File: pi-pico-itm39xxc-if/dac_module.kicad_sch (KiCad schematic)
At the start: 52 parts

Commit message: Working on pico itm interface
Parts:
- removed C? (x2): 1uF, Capacitor_SMD:C_0805_2012Metric, symbol Device:C_Small
- removed C?: 100nF, Capacitor_SMD:C_0805_2012Metric, symbol Device:C_Small
- removed U?: MAX6035xxUR25, Package_TO_SOT_SMD:SOT-23_Handsoldering, symbol Reference_Voltage:MAX6035xxUR25
- added C?: 100nF, Capacitor_SMD:C_0805_2012Metric, symbol Device:C_Small
- added R?: 2k, Resistor_SMD:R_0805_2012Metric, symbol Device:R_Small
- added U?: LM4040DBZ-3, Package_TO_SOT_SMD:SOT-23, symbol Reference_Voltage:LM4040DBZ-3
- C?: value 150nF -> 1uF
- R? (x4): value 30k -> 56k
- R?: value 47k -> 10k
- R? (x4): value 10k -> 24k
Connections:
- net GND: now also C?.2, U?.2 (A)
- net Vdd: now also R?.1
- net at U?.3 (+): now also C?.1, R?.2, U?.1 (K)
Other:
- note added: "Supply info - Vdd: 3.3 V - Vcc: 12 V Analog outputs: - DAC_A1, A2 and A3: 0 V - 10 V - DAC_REF: 3 V [1] Although MCP4922's does not seem to specify some minimum output load, we place a resistor here. This is also done in mikroe's MCP4921 board: https://download.mikroe.com/documents/add-on-boards/click/dac/dac-click-schematic-v100.pdf [2] LM4040's datasheet recommends a 100nF bypass cap at the cat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"
- note removed: "Supply info - Vdd: 3.3 V - Vcc: 12 V Analog outputs: - 0 V - 10 V [1] Although MCP4922's does not seem to specify some minimum output load, we place a resistor here. This is also done in mikroe's MCP4921 board: https://download.mikroe.com/documents/add-on-boards/click/dac/dac-click-schematic-v100.pdf [2] This load capacitor might be required by some voltage references, for example MCP1525. [3] Si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"
- moved on the sheet: C?, R?, U?A, U?B, U?C

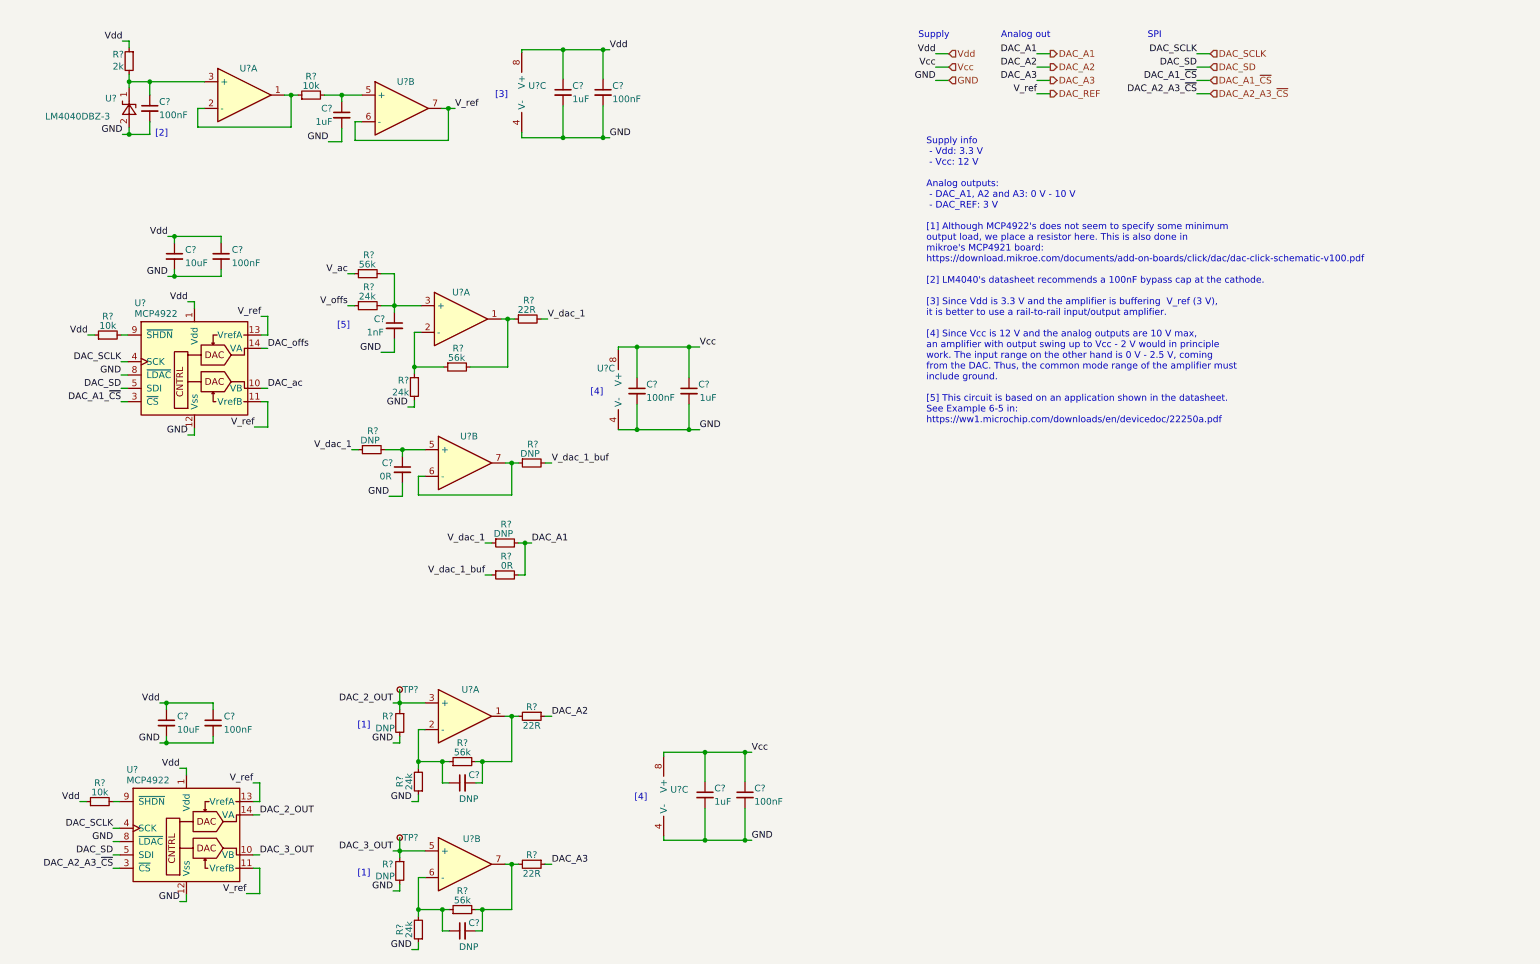
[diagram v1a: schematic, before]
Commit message: Added docs for subcircuits
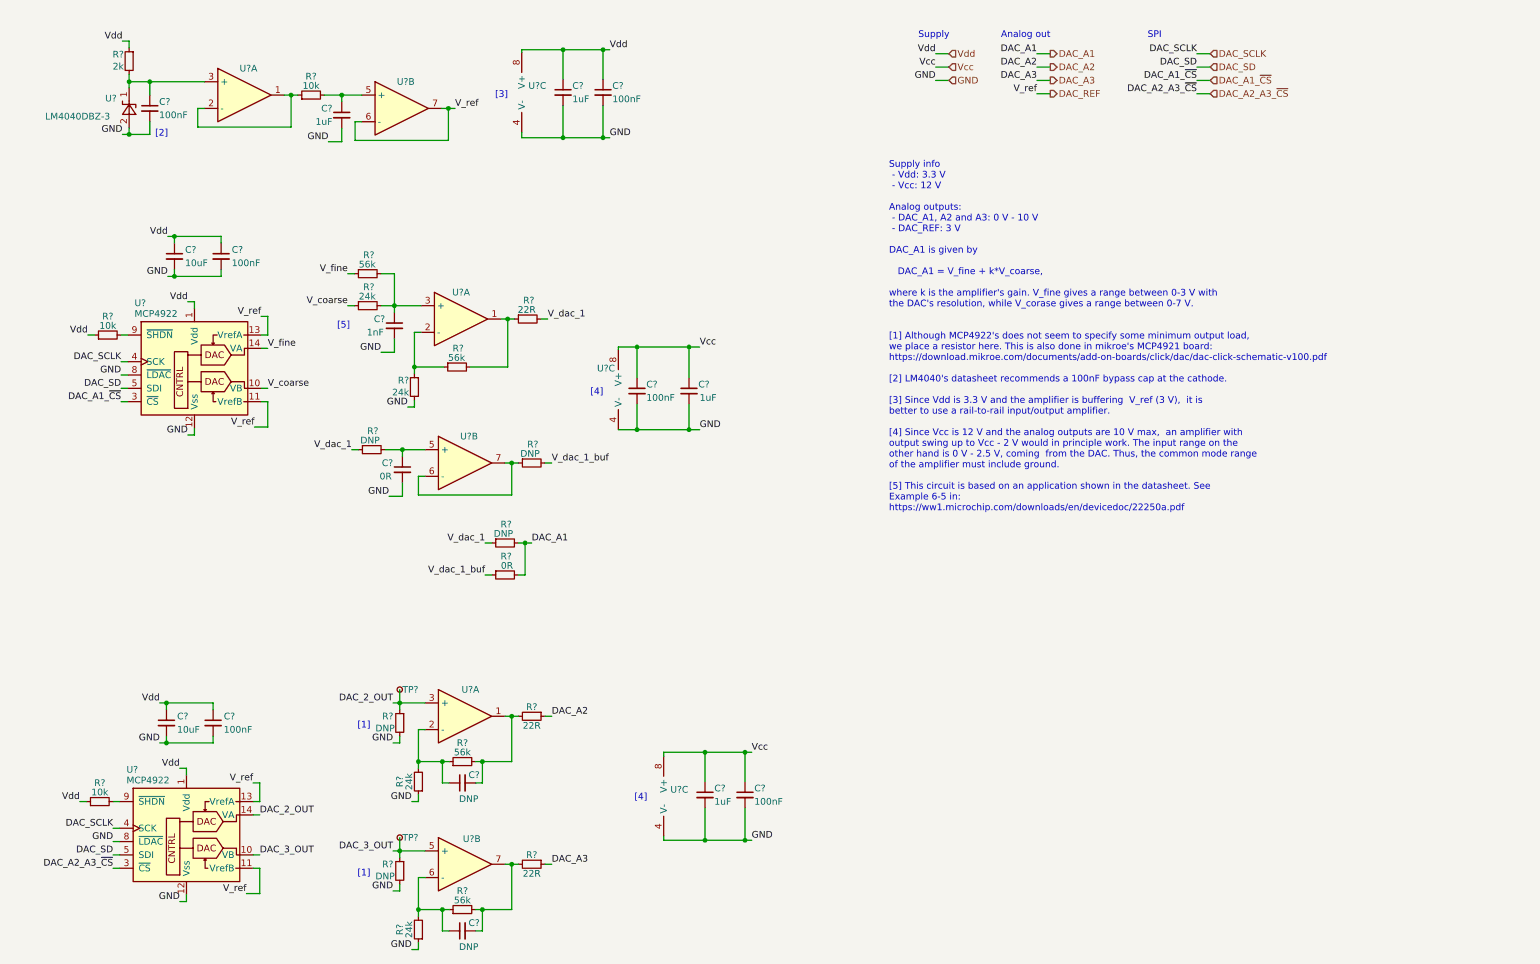
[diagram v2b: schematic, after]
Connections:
- net V_ac is gone; now on net V_fine: R?.1
- net V_offs is gone; now on net V_coarse: R?.1
- net DAC_ac renamed V_coarse
- net DAC_offs renamed V_fine
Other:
- note added: "Supply info - Vdd: 3.3 V - Vcc: 12 V Analog outputs: - DAC_A1, A2 and A3: 0 V - 10 V - DAC_REF: 3 V DAC_A1 is given by DAC_A1 = V_fine + k*V_coarse, where k is the amplifier's gain. V_fine gives a range between 0-3 V with the DAC's resolution, while V_corase gives a range between 0-7 V. [1] Although MCP4922's does not seem to specify some minimum output load, we place a resistor here. This is als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"
- note removed: "Supply info - Vdd: 3.3 V - Vcc: 12 V Analog outputs: - DAC_A1, A2 and A3: 0 V - 10 V - DAC_REF: 3 V [1] Although MCP4922's does not seem to specify some minimum output load, we place a resistor here. This is also done in mikroe's MCP4921 board: https://download.mikroe.com/documents/add-on-boards/click/dac/dac-click-schematic-v100.pdf [2] LM4040's datasheet recommends a 100nF bypass cap at the cat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"
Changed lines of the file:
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@@
     (effects (font (size 1.27 1.27)) (justify right bottom))
   )
-  (text "Supply info\n - Vdd: 3.3 V\n - Vcc: 12 V\n\nAnalog outputs:\n - DAC_A1, A2 and A3: 0 V - 10 V\n - DAC_REF: 3 V\n\n[1] Although MCP4922's does not seem to specify some minimum\noutput load, we place a resistor here. This is also done in\nmikroe's MCP4921 board:\nhttps://download.mikroe.com/documents/add-on-boards/click/dac/dac-click-schematic-v100.pdf\n\n[2] LM4040's datasheet recommends a 100nF bypass cap at the cathode.\n\n[3] Since Vdd is 3.3 V and the amplifier is buffering  V_ref (3 V), \nit is better to use a rail-to-rail input/output amplifier.\n\n[4] Since Vcc is 12 V and the analog outputs are 10 V max, \nan amplifier with output swing up to Vcc - 2 V would in principle\nwork. The input range on the other hand is 0 V - 2.5 V, coming \nfrom the DAC. Thus, the common mode range of the amplifier must \ninclude ground. \n\n[5] This circuit is based on an application shown in the datasheet.\nSee Example 6-5 in:\nhttps://ww1.microchip.com/downloads/en/devicedoc/22250a.pdf"
-    (at 183.388 92.456 0)
+  (text "Supply info\n - Vdd: 3.3 V\n - Vcc: 12 V\n\nAnalog outputs:\n - DAC_A1, A2 and A3: 0 V - 10 V\n - DAC_REF: 3 V\n\nDAC_A1 is given by\n\n   DAC_A1 = V_fine + k*V_coarse,\n\nwhere k is the amplifier's gain. V_fine gives a range between 0-3 V with\nthe DAC's resolution, while V_corase gives a range between 0-7 V.\n\n\n[1] Although MCP4922's does not seem to specify some minimum output load, \nwe place a resistor here. This is also done in mikroe's MCP4921 board:\nhttps://download.mikroe.com/documents/add-on-boards/click/dac/dac-click-schematic-v100.pdf\n\n[2] LM4040's datasheet recommends a 100nF bypass cap at the cathode.\n\n[3] Since Vdd is 3.3 V and the amplifier is buffering  V_ref (3 V),  it is \nbetter to use a rail-to-rail input/output amplifier.\n\n[4] Since Vcc is 12 V and the analog outputs are 10 V max,  an amplifier with\noutput swing up to Vcc - 2 V would in principle work. The input range on the\nother hand is 0 V - 2.5 V, coming  from the DAC. Thus, the common mode range \nof the amplifier must include ground. \n\n[5] This circuit is based on an application shown in the datasheet. See \nExample 6-5 in:\nhttps://ww1.microchip.com/downloads/en/devicedoc/22250a.pdf"
+    (at 176.276 109.22 0)
     (effects (font (size 1.27 1.27)) (justify left bottom))
   )
@@
     (effects (font (size 1.27 1.27)) (justify right bottom))
   )
-  (label "V_ac" (at 73.152 63.754 180)
+  (label "V_fine" (at 73.152 63.754 180)
     (effects (font (size 1.27 1.27)) (justify right bottom))
   )
@@
     (effects (font (size 1.27 1.27)) (justify left bottom))
   )
-  (label "DAC_ac" (at 57.912 85.598 0)
+  (label "V_coarse" (at 57.912 85.598 0)
     (effects (font (size 1.27 1.27)) (justify left bottom))
   )
@@
     (effects (font (size 1.27 1.27)) (justify left bottom))
   )
-  (label "DAC_offs" (at 57.912 77.978 0)
+  (label "V_fine" (at 57.912 77.978 0)
     (effects (font (size 1.27 1.27)) (justify left bottom))
   )
@@
     (effects (font (size 1.27 1.27)) (justify right bottom))
   )
-  (label "V_offs" (at 73.152 69.85 180)
-    (effects (font (size 1.27 1.27)) (justify right bottom))
-  )
+  (label "V_coarse" (at 73.152 69.85 180)
+    (effects (font (size 1.27 1.27)) (justify right bottom))
+  )

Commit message: Passing ERC
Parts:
- C16, C17, C18, C19, C22, C23, C24, C25, C28, C29, C30, C31: renamed from C?; footprint Capacitor_SMD:C_0805_2012Metric -> Capacitor_SMD:C_0805_2012Metric_Pad1.18x1.45mm_HandSolder
- R15, R17, R18, R19, R21, R22, R23, R24, R25, R26: renamed from R?; footprint Resistor_SMD:R_0805_2012Metric -> Resistor_SMD:R_0805_2012Metric_Pad1.20x1.40mm_HandSolder
- U8: renamed from U?; footprint (none) -> Package_SO:SOIC-8_3.9x4.9mm_P1.27mm
- gave numbers to parts that had none: 22

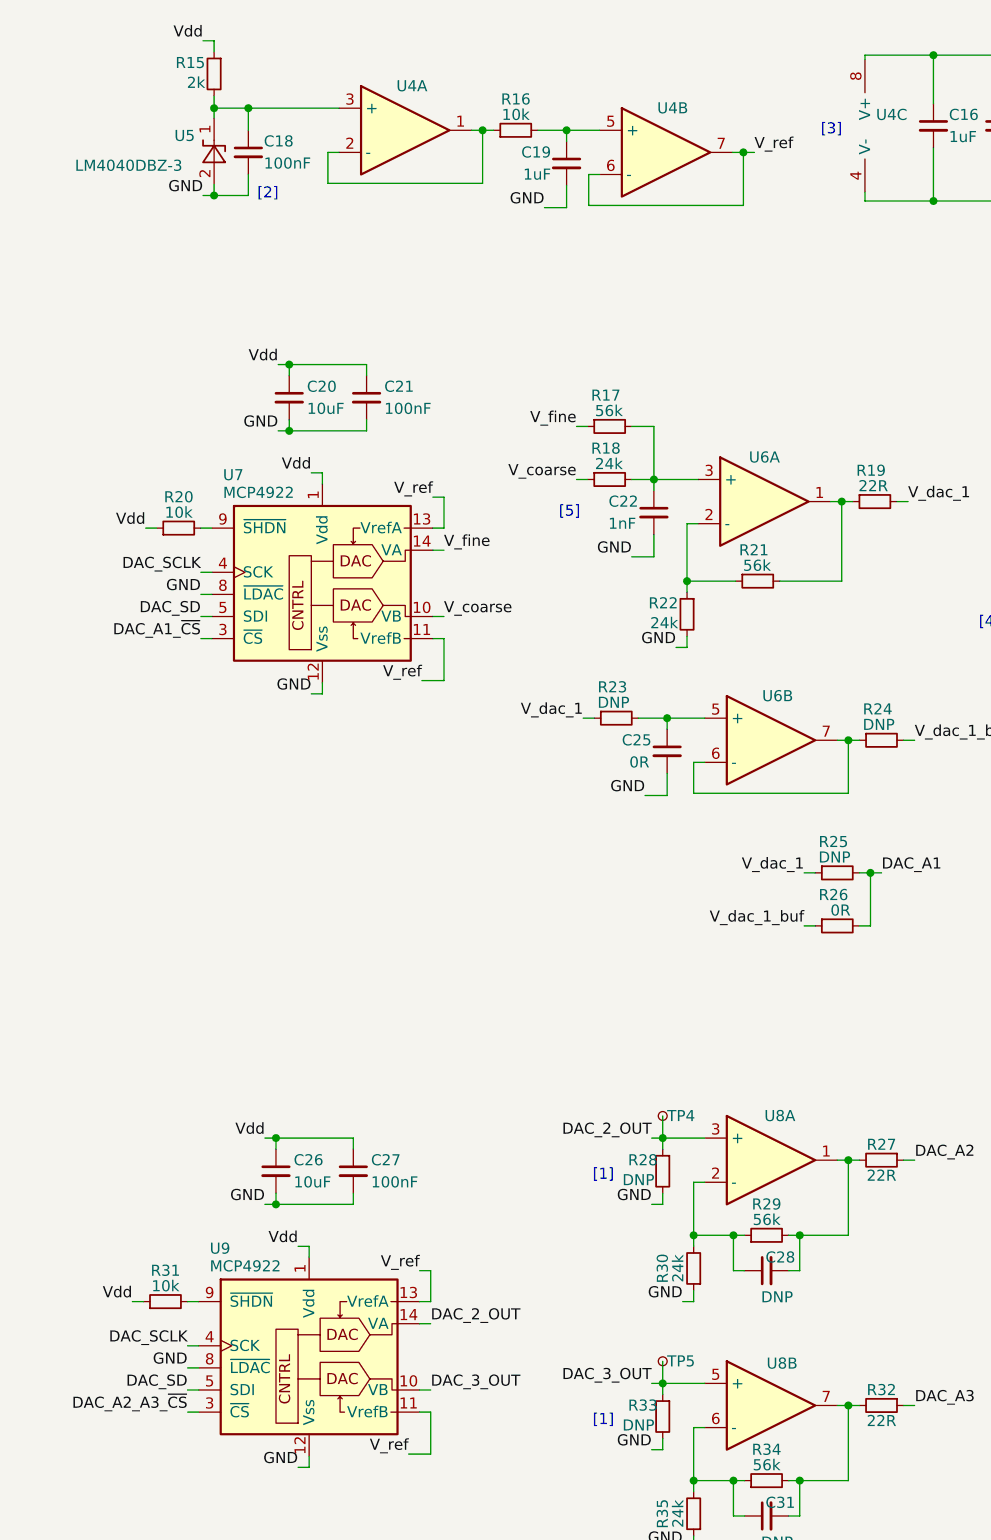
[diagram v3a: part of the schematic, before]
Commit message: Working on pcb for pi pico it
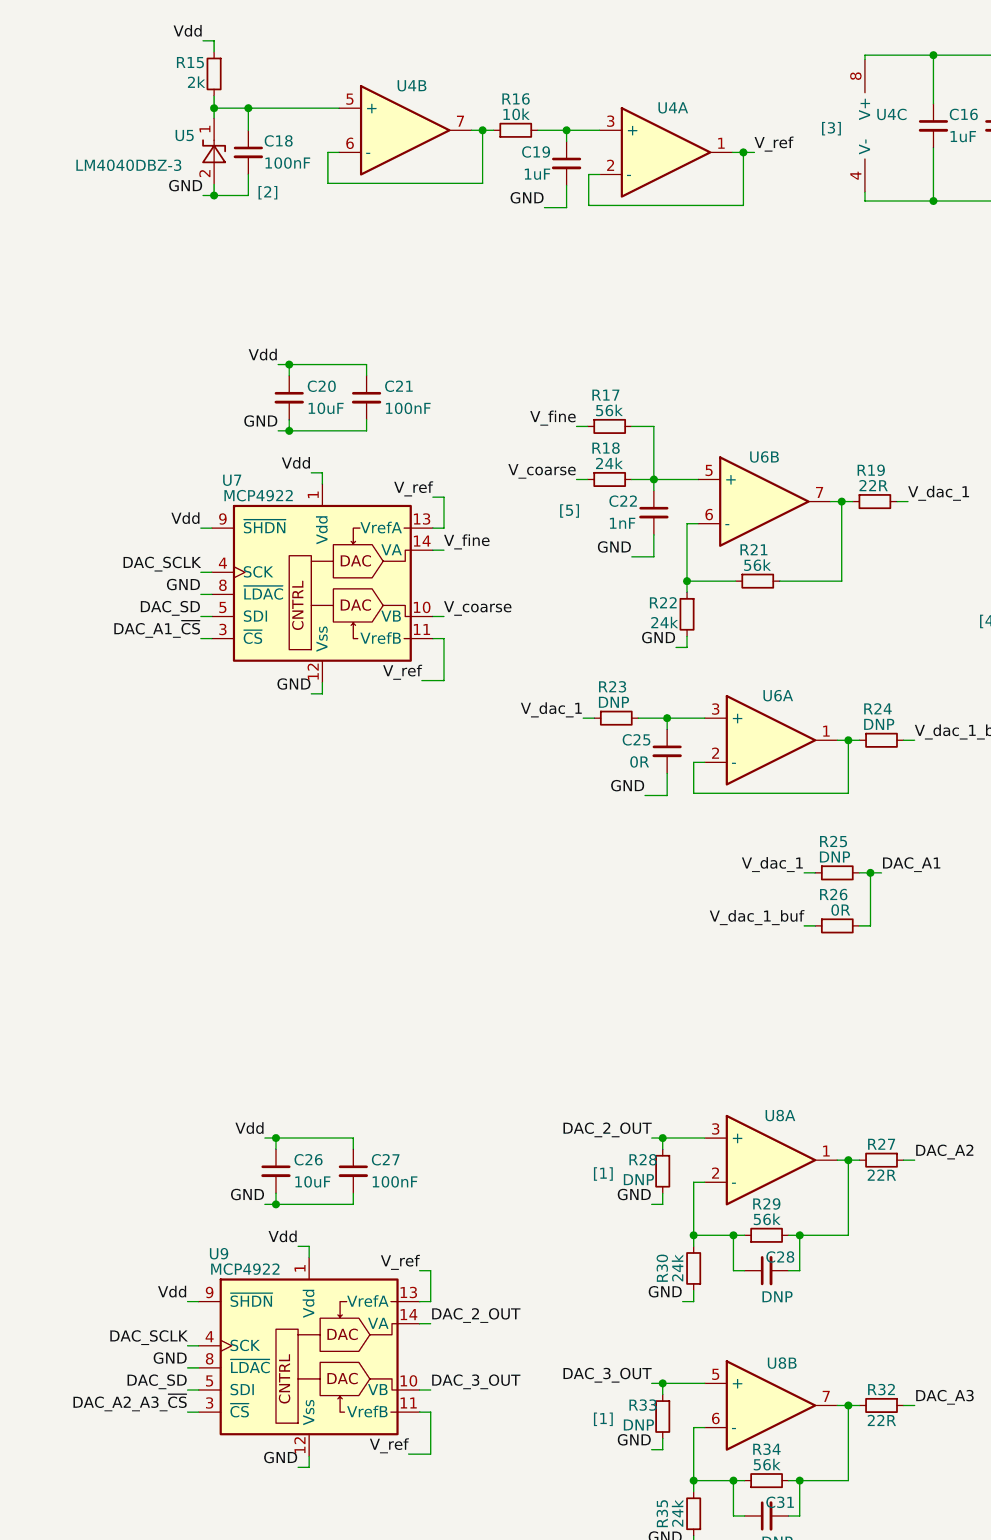
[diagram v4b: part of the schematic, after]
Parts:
- removed R20, R31: 10k, Resistor_SMD:R_0805_2012Metric_Pad1.20x1.40mm_HandSolder, symbol Device:R_Small
- removed TP4, TP5: TestPoint_Small, TestPoint:TestPoint_Pad_2.0x2.0mm, symbol Connector:TestPoint_Small
- removed U7, U9: MCP4922, Package_SO:SOIC-16_3.9x9.9mm_P1.27mm, symbol Analog_DAC:MCP4922
- added U7, U9: MCP4922, Package_SO:SOIC-14_3.9x8.7mm_P1.27mm, symbol CL_Analog_DAC:MCP4922
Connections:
- net DAC_2_OUT: now also U9.14 (VA)
- net DAC_3_OUT: now also U9.10 (VB)
- net DAC_A1_~{CS}: now also U7.3 (~{CS})
- net DAC_A2_A3_~{CS}: now also U9.3 (~{CS})
- net DAC_REF: now also U4.1, U4.2 (-), U7.11 (VrefB), U7.13 (VrefA), U9.11 (VrefB), U9.13 (VrefA); no longer U4.6 (-), U4.7
- net DAC_SCLK: now also U7.4 (SCK), U9.4 (SCK)
- net DAC_SD: now also U7.5 (SDI), U9.5 (SDI)
- net GND: now also U7.12 (Vss), U7.8 (~{LDAC}), U9.12 (Vss), U9.8 (~{LDAC})
- net V_coarse: now also U7.10 (VB)
- net V_fine: now also U7.14 (VA)
- net Vdd: now also U7.1 (Vdd), U7.9 (~{SHDN}), U9.1 (Vdd), U9.9 (~{SHDN})
- net at C18.1, R15.2, U5.1 (K): now also U4.5 (+); no longer U4.3 (+)
- net at C19.1, R16.2: now also U4.3 (+); no longer U4.5 (+)
- net at C25.1, R23.2: now also U6.3 (+); no longer U6.5 (+)
- net at C22.1, R17.2, R18.2: now also U6.5 (+); no longer U6.3 (+)
- net at R19.1, R21.2: now also U6.7; no longer U6.1
- net at R21.1, R22.1: now also U6.6 (-); no longer U6.2 (-)
- new net: R16.1, U4.6 (-), U4.7
- new net: R24.1, U6.1, U6.2 (-)
